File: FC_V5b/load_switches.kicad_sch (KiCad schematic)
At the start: 51 parts, among them U19 AP22652, U21 AP22652, U22 AP22652, U23 AP22652, U24 AP22652, U25 TPS2HB50AQPWPRQ1, U29 AP22652, U6 TPS4H160AQPWPRQ1

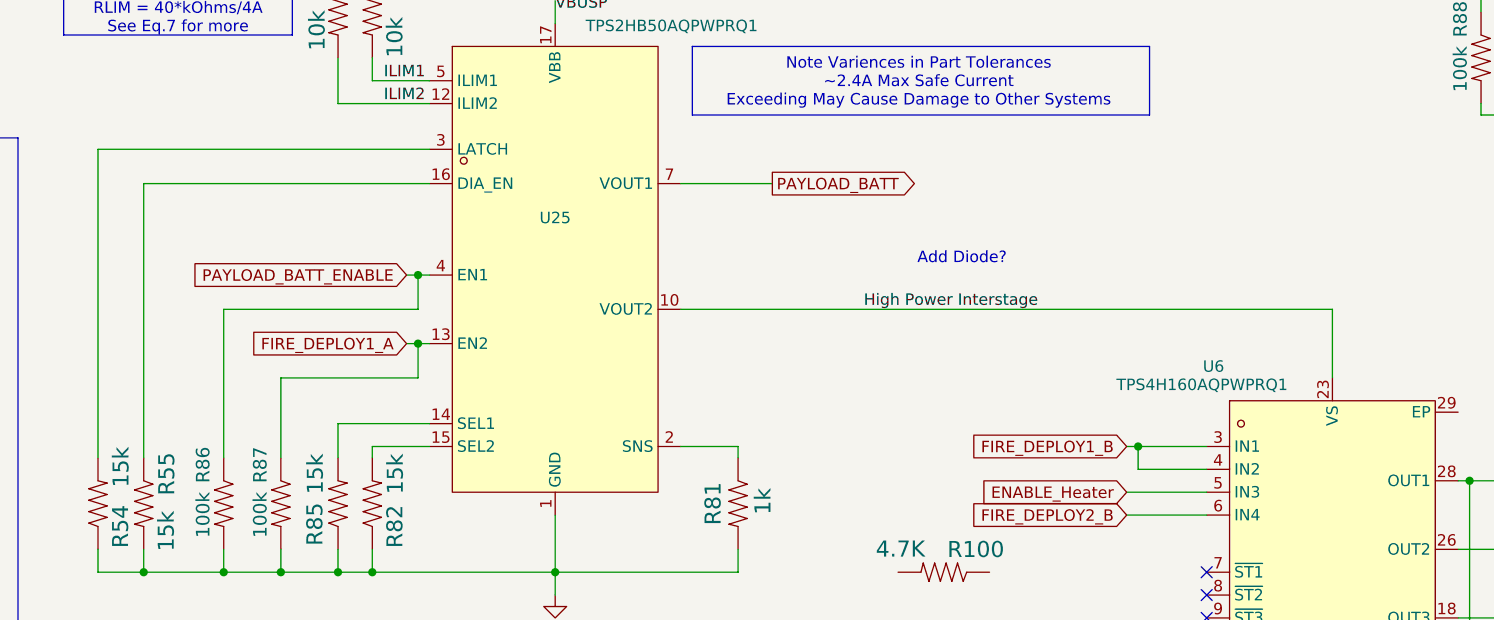
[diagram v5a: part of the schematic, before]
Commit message: Repositioned Sys INA and Removed VBUSP TP
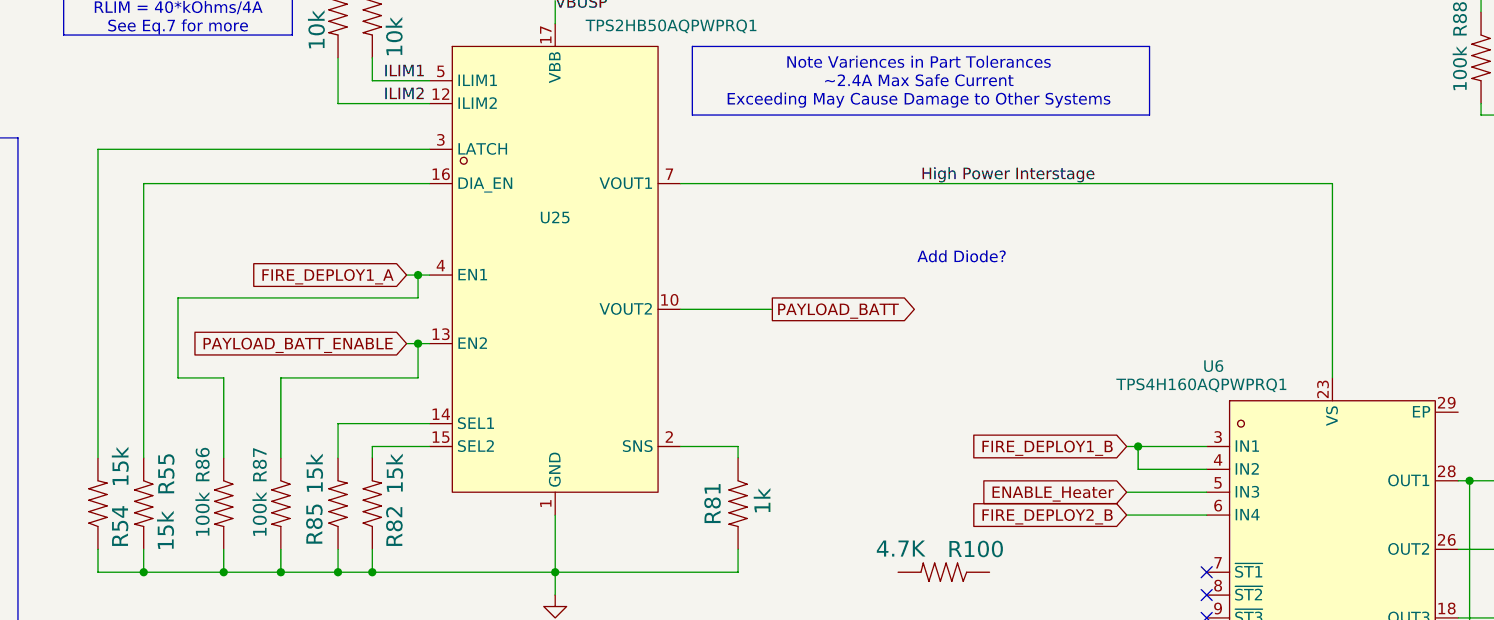
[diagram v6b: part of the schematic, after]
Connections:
- net FIRE_DEPLOY1_A: now also R86.1, U25.4 (EN1); no longer R87.1, U25.13 (EN2)
- net High Power Interstage: now also U25.6 (VOUT1), U25.7 (VOUT1), U25.8 (VOUT1); no longer U25.10 (VOUT2), U25.11 (VOUT2), U25.9 (VOUT2)
- net PAYLOAD_BATT: now also U25.10 (VOUT2), U25.11 (VOUT2), U25.9 (VOUT2); no longer U25.6 (VOUT1), U25.7 (VOUT1), U25.8 (VOUT1)
- net PAYLOAD_BATT_ENABLE: now also R87.1, U25.13 (EN2); no longer R86.1, U25.4 (EN1)
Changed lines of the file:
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@@
-	(wire
-		(pts
-			(xy 247.65 66.04) (xy 247.65 73.66)
-		)
-		(stroke
-			(width 0)
-			(type default)
-		)
-	)
 	(wire
 		(pts
@@
 	(wire
 		(pts
-			(xy 124.46 66.04) (xy 124.46 82.55)
+			(xy 119.38 64.77) (xy 119.38 73.66)
 		)
 		(stroke
@@
 	(wire
 		(pts
-			(xy 146.05 62.23) (xy 146.05 66.04)
+			(xy 146.05 62.23) (xy 146.05 64.77)
 		)
 		(stroke
@@
 	(wire
 		(pts
-			(xy 175.26 66.04) (xy 247.65 66.04)
-		)
-		(stroke
-			(width 0)
-			(type default)
-		)
-	)
-	(wire
-		(pts
 			(xy 161.29 88.9) (xy 161.29 95.25)
 		)
@@
 	(wire
 		(pts
-			(xy 175.26 52.07) (xy 185.42 52.07)
-		)
-		(stroke
-			(width 0)
-			(type default)
-		)
-	)
-	(wire
-		(pts
 			(xy 224.79 88.9) (xy 233.68 88.9)
 		)
@@
 	(wire
 		(pts
+			(xy 247.65 52.07) (xy 247.65 73.66)
+		)
+		(stroke
+			(width 0)
+			(type default)
+		)
+	)
+	(wire
+		(pts
 			(xy 123.19 171.45) (xy 133.35 171.45)
 		)
@@
 	(wire
 		(pts
-			(xy 146.05 66.04) (xy 124.46 66.04)
+			(xy 146.05 64.77) (xy 119.38 64.77)
 		)
 		(stroke
@@
 	(wire
 		(pts
+			(xy 175.26 66.04) (xy 185.42 66.04)
+		)
+		(stroke
+			(width 0)
+			(type default)
+		)
+	)
+	(wire
+		(pts
 			(xy 128.27 166.37) (xy 128.27 163.83)
 		)
@@
 	(wire
 		(pts
+			(xy 124.46 73.66) (xy 124.46 82.55)
+		)
+		(stroke
+			(width 0)
+			(type default)
+		)
+	)
+	(wire
+		(pts
 			(xy 124.46 95.25) (xy 130.81 95.25)
 		)
@@
 	(wire
 		(pts
+			(xy 119.38 73.66) (xy 124.46 73.66)
+		)
+		(stroke
+			(width 0)
+			(type default)
+		)
+	)
+	(wire
+		(pts
 			(xy 226.06 81.28) (xy 233.68 81.28)
 		)
@@
 	(wire
 		(pts
+			(xy 247.65 52.07) (xy 175.26 52.07)
+		)
+		(stroke
+			(width 0)
+			(type default)
+		)
+	)
+	(wire
+		(pts
 			(xy 73.66 170.18) (xy 78.74 170.18)
 		)
@@
 	)
 	(label "High Power Interstage"
-		(at 195.58 66.04 0)
+		(at 201.93 52.07 0)
 		(effects
 			(font
@@
 		)
 	)
-	(global_label "FIRE_DEPLOY1_A"
-		(shape input)
-		(at 144.78 69.85 180)
-		(fields_autoplaced yes)
-		(effects
-			(font
-				(size 1.27 1.27)
-			)
-			(justify right)
-		)
-		(property "Intersheetrefs" "${INTERSHEET_REFS}"
-			(at 126.3129 69.85 0)
-			(effects
-				(font
-					(size 1.27 1.27)
-				)
-				(justify right)
-				(hide yes)
-			)
-		)
-	)
 	(global_label "F3_PWR"
 		(shape output)
@@
 		)
 	)
-	(global_label "PAYLOAD_BATT_ENABLE"
-		(shape input)
-		(at 144.78 62.23 180)
-		(fields_autoplaced yes)
-		(effects
-			(font
-				(size 1.27 1.27)
-			)
-			(justify right)
-		)
-		(property "Intersheetrefs" "${INTERSHEET_REFS}"
-			(at 120.3862 62.23 0)
-			(effects
-				(font
-					(size 1.27 1.27)
-				)
-				(justify right)
-				(hide yes)
-			)
-		)
-	)
 	(global_label "~{FACE1_ENABLE}"
 		(shape input)
@@
 		)
 	)
+	(global_label "PAYLOAD_BATT"
+		(shape output)
+		(at 185.42 66.04 0)
+		(fields_autoplaced yes)
+		(effects
+			(font
+				(size 1.27 1.27)
+			)
+			(justify left)
+		)
+		(property "Intersheetrefs" "${INTERSHEET_REFS}"
+			(at 201.831 66.04 0)
+			(effects
+				(font
+					(size 1.27 1.27)
+				)
+				(justify left)
+				(hide yes)
+			)
+		)
+	)
+	(global_label "PAYLOAD_BATT_ENABLE"
+		(shape input)
+		(at 144.78 69.85 180)
+		(fields_autoplaced yes)
+		(effects
+			(font
+				(size 1.27 1.27)
+			)
+			(justify right)
+		)
+		(property "Intersheetrefs" "${INTERSHEET_REFS}"
+			(at 120.3862 69.85 0)
+			(effects
+				(font
+					(size 1.27 1.27)
+				)
+				(justify right)
+				(hide yes)
+			)
+		)
+	)
 	(global_label "~{FACE4_ENABLE}"
 		(shape input)
@@
 		)
 	)
+	(global_label "FIRE_DEPLOY1_A"
+		(shape input)
+		(at 144.78 62.23 180)
+		(fields_autoplaced yes)
+		(effects
+			(font
+				(size 1.27 1.27)
+			)
+			(justify right)
+		)
+		(property "Intersheetrefs" "${INTERSHEET_REFS}"
+			(at 126.3129 62.23 0)
+			(effects
+				(font
+					(size 1.27 1.27)
+				)
+				(justify right)
+				(hide yes)
+			)
+		)
+	)
 	(global_label "~{FACE2_ENABLE}"
 		(shape input)
@@
 			(effects
 				(font
-					(size 1.27 1.27)
-				)
-				(justify left)
-				(hide yes)
-			)
-		)
-	)
-	(global_label "PAYLOAD_BATT"
-		(shape output)
-		(at 185.42 52.07 0)
-		(fields_autoplaced yes)
-		(effects
-			(font
-				(size 1.27 1.27)
-			)
-			(justify left)
-		)
-		(property "Intersheetrefs" "${INTERSHEET_REFS}"
-			(at 201.831 52.07 0)
-			(effects
-				(font

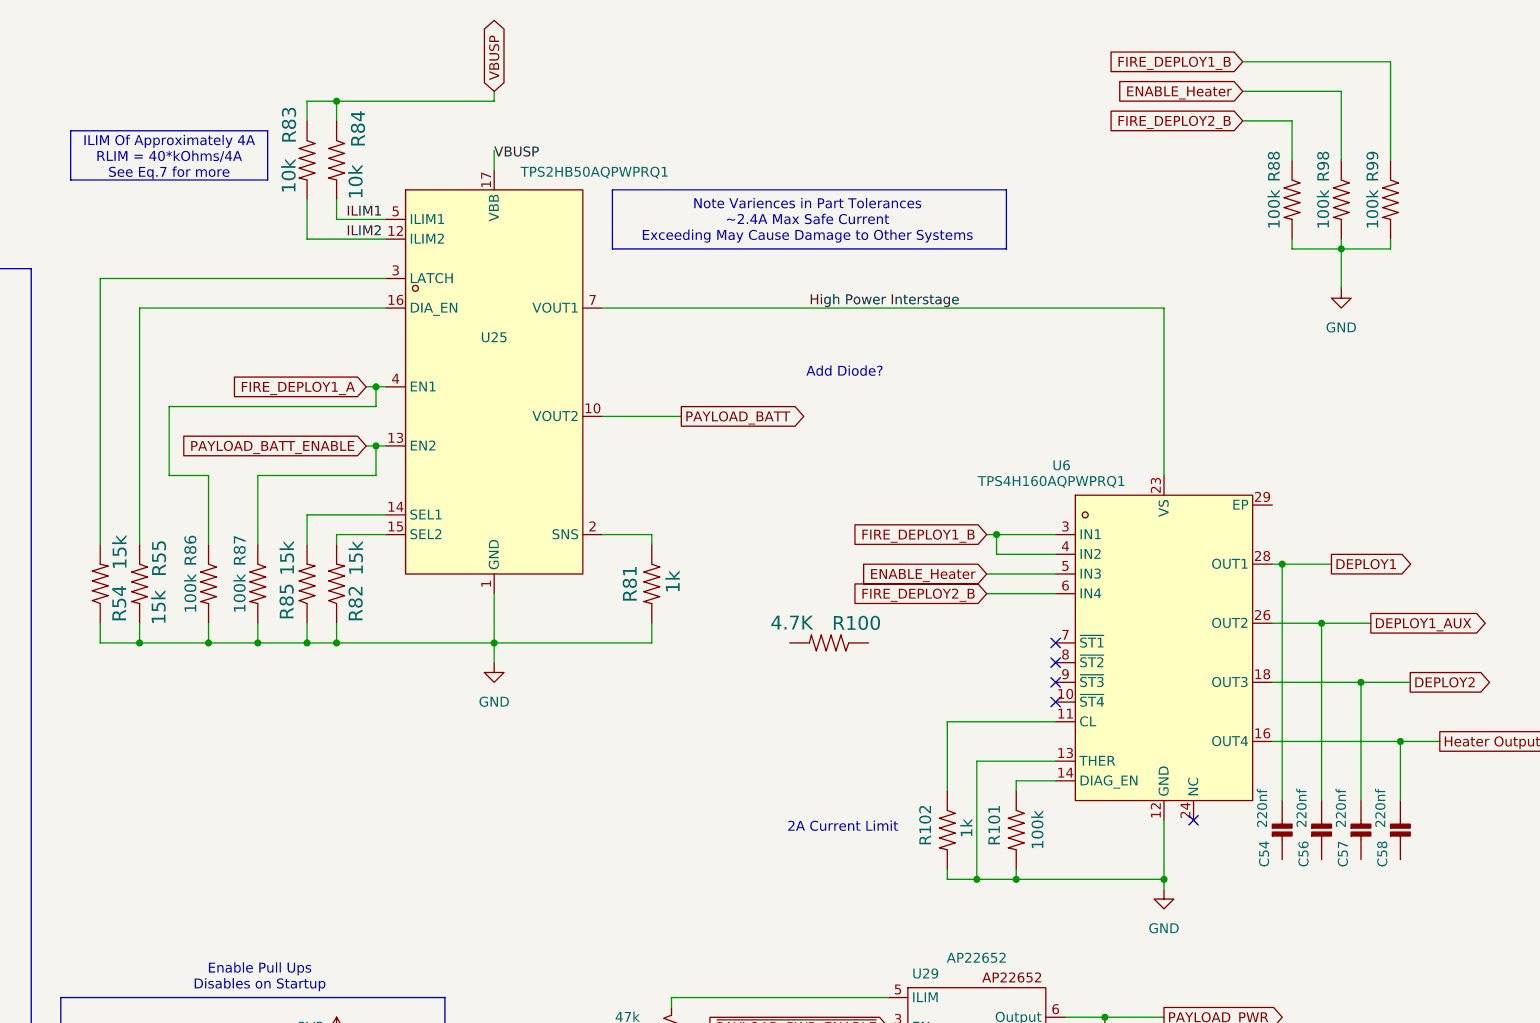
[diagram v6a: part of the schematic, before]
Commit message: Completed Layout of New TSP2 and TPS4 Load Switches
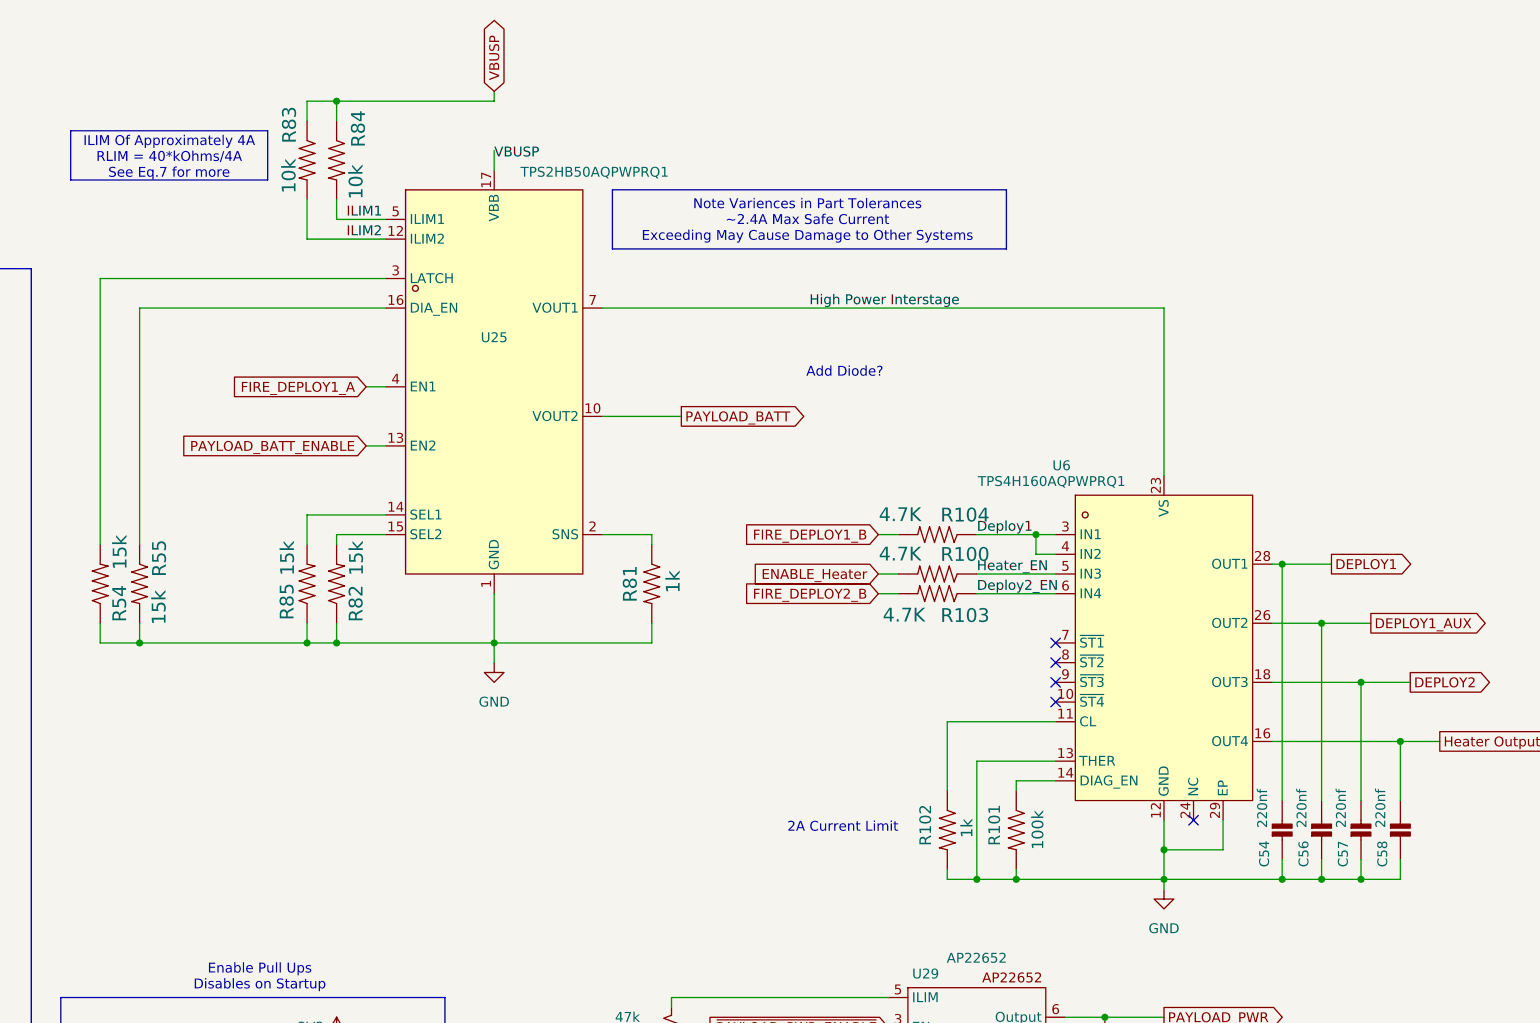
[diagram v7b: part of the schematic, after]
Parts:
- removed R86, R87, R88, R98, R99: 100k, Resistor_SMD:R_0603_1608Metric, symbol mainboard:R-US_R0603
- added R103, R104: 4.7K, Resistor_SMD:R_0603_1608Metric, symbol mainboard:RESISTOR0603
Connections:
- net ENABLE_Heater: now also R100.2; no longer U6.5 (IN3)
- net FIRE_DEPLOY1_B: now also R104.2; no longer U6.3 (IN1), U6.4 (IN2)
- net FIRE_DEPLOY2_B: now also R103.2; no longer U6.6 (IN4)
- net GND: now also C54.2, C56.2, C57.2, C58.2, U6.29 (EP)
- net Heater_EN: now reaches R100.1
- net Heater_EN: now also U6.5 (IN3)
- new net Deploy1: R104.1, U6.3 (IN1), U6.4 (IN2)
- new net Deploy2_EN: R103.1, U6.6 (IN4)
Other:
- moved on the sheet: R100
